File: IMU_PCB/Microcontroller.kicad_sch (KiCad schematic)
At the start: 17 parts, among them J4 Conn_01x02_Pin, M3 MountingHole, M3_1 MountingHole, U2 ESP32-DEVKIT-C, U3 TJA1050T/CM,118

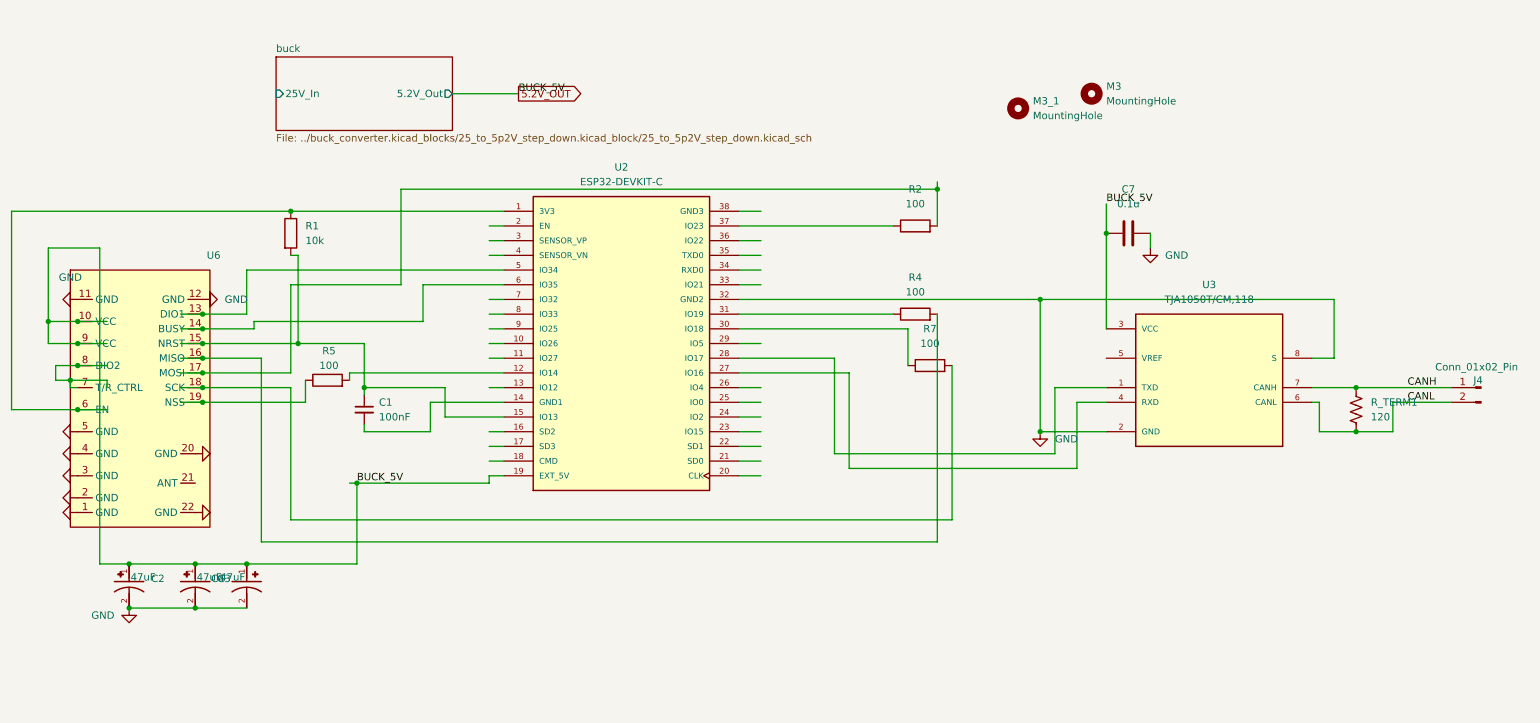
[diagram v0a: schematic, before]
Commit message: updated Julias IMU to use the revised buck converter and connectors. made the back plane mostly a ground plane (for the buck converter)
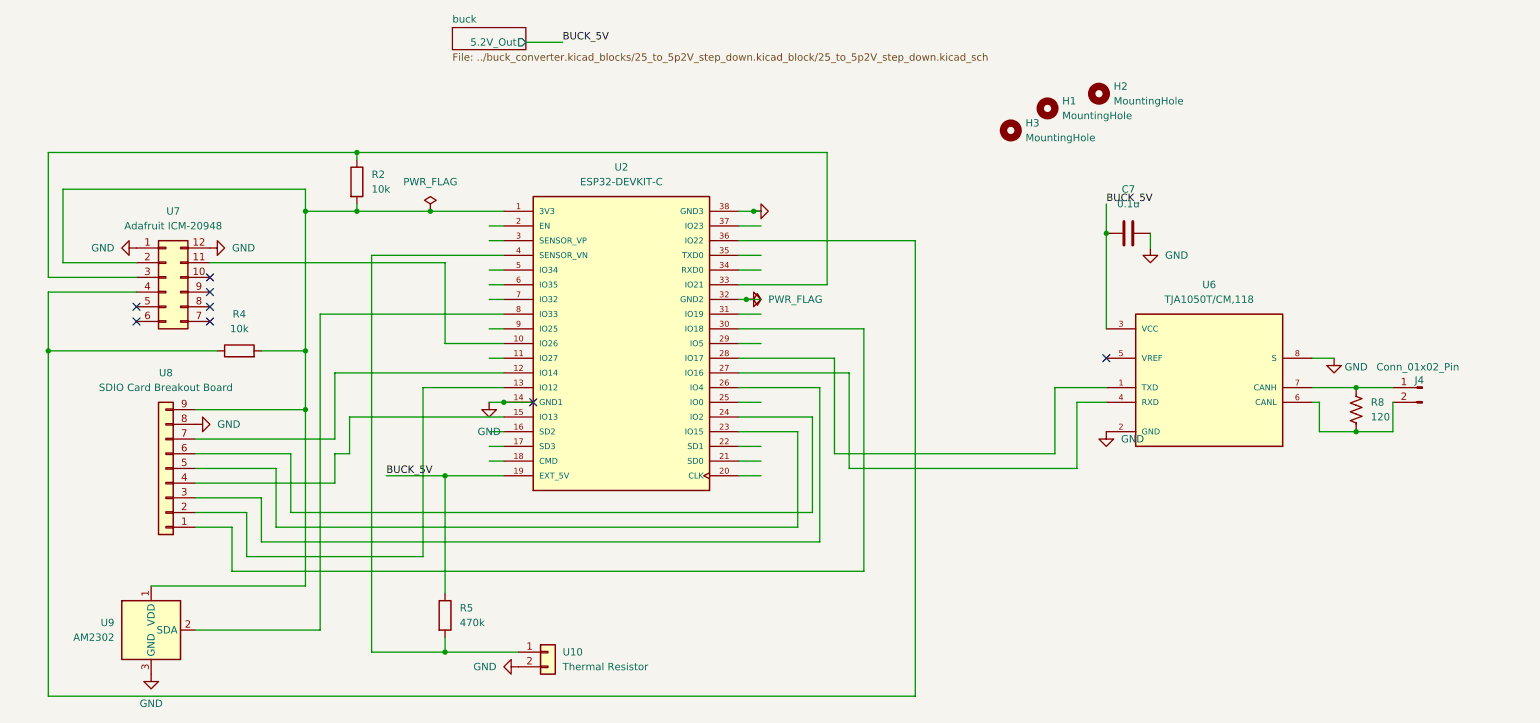
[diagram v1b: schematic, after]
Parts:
- removed C1: 100nF, Capacitor_SMD:C_1206_3216Metric_Pad1.33x1.80mm_HandSolder, symbol Device:C_Small
- removed C2, C3, C4: 47uF, Capacitor_Tantalum_SMD:CP_EIA-3528-21_Kemet-B_HandSolder, symbol 10TPE47MAZB:10TPE47MAZB
- removed M3, M3_1: MountingHole, MountingHole:MountingHole_3.2mm_M3, symbol Mechanical:MountingHole
- removed R1: 10k, Resistor_SMD:R_1206_3216Metric_Pad1.30x1.75mm_HandSolder, symbol Device:R
- removed R7: 100, Resistor_SMD:R_1206_3216Metric_Pad1.30x1.75mm_HandSolder, symbol Device:R
- removed U6: (no value), PROVE-footprints:E22P-915M30S, symbol telem_linsym:E22P-915M30S
- added H1, H2, H3: MountingHole, MountingHole:MountingHole_3.2mm_M3, symbol Mechanical:MountingHole
- added U10: Thermal Resistor, TerminalBlock_RND:TerminalBlock_RND_205-00232_1x02_P5.08mm_Horizontal, symbol Connector_Generic:Conn_01x02
- added U7: Adafruit ICM-20948, PROVE-footprints:Adafruit_ICM20948_2x6_Module, symbol Connector_Generic:Conn_02x06_Counter_Clockwise
- added U8: SDIO Card Breakout Board, Connector_PinHeader_2.54mm:PinHeader_1x09_P2.54mm_Vertical, symbol Connector_Generic:Conn_01x09
- added U9: AM2302, Sensor:ASAIR_AM2302_P2.54mm_Vertical, symbol Sensor:AM2302
- R2, R4: value 100 -> 10k; footprint Resistor_SMD:R_1206_3216Metric_Pad1.30x1.75mm_HandSolder -> Resistor_SMD:R_0805_2012Metric
- R5: value 100 -> 470k; footprint Resistor_SMD:R_1206_3216Metric_Pad1.30x1.75mm_HandSolder -> Resistor_SMD:R_0805_2012Metric
- U2: MANUFACTURER (none) -> ESPRESSIF
- U6: renamed from U3; MANUFACTURER (none) -> NXP USA
- renumbered R_TERM1 to R8
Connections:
- net 5.2V_OUT is gone; now on net BUCK_5V: C7.2, U2.19 (EXT_5V), U6.3 (VCC)
- net GND: now also U2.14 (GND1), U2.38 (GND3), U10.2 (Pin_2), U7.1 (Pin_1), U7.12 (Pin_12), U8.8 (Pin_8), U9.3 (GND), U9.4 (GND)
- net at U2.1 (3V3): now also R2.2, R4.2, U7.2 (Pin_2), U8.9 (Pin_9), U9.1 (VDD)
- net at U2.15 (IO13): now also U8.4 (Pin_4)
- net BUCK_5V: now reaches R5.1
- net at R2.1: now also U2.33 (IO21), U7.3 (Pin_3); no longer U2.37 (IO23)
- net at U2.30 (IO18): now also U8.1 (Pin_1)
- net at U2.12 (IO14): now also U8.7 (Pin_7); no longer R5.2
- net at U2.10 (IO26): now also U7.11 (Pin_11)
- net at U2.13 (IO12): now also U8.2 (Pin_2)
- net at U2.23 (IO15): now also U8.5 (Pin_5)
- net at U2.24 (IO2): now also U8.6 (Pin_6)
- net at U2.26 (IO4): now also U8.3 (Pin_3)
- net at R4.1: now also U2.36 (IO22), U7.4 (Pin_4); no longer U2.31 (IO19)
- net at U2.4 (SENSOR_VN): now also R5.2, U10.1 (Pin_1)
- net at U2.8 (IO33): now also U9.2 (SDA)
- net CANH: no longer names the net of J4.1 (Pin_1), R8.1, U6.7 (CANH)
- net CANL: no longer names the net of J4.2 (Pin_2), R8.2, U6.6 (CANL)
- no-connect marks 0 -> 8
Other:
- sheet buck ports: added none; removed 25V_In
- company: (none) -> PROVE Lab, Julia Kohrt
- title: (none) -> IMU Board
- moved on the sheet: J4

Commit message: small updates to buck, fixed vias, and remove connection to input connector ground pad
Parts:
- removed H2: MountingHole, MountingHole:MountingHole_3.2mm_M3, symbol Mechanical:MountingHole
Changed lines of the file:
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@@
-	(symbol
-		(lib_id "Mechanical:MountingHole")
-		(at 203.2 88.9 0)
-		(unit 1)
-		(body_style 1)
-		(exclude_from_sim no)
-		(in_bom no)
-		(on_board yes)
-		(in_pos_files yes)
-		(dnp no)
-		(fields_autoplaced yes)
-		(property "Reference" "H2"
-			(at 205.74 87.6299 0)
-			(show_name no)
-			(do_not_autoplace no)
-			(effects
-				(font
-					(size 1.27 1.27)
-				)
-				(justify left)
-			)
-		)
-		(property "Value" "MountingHole"
-			(at 205.74 90.1699 0)
-			(show_name no)
-			(do_not_autoplace no)
-			(effects
-				(font
-					(size 1.27 1.27)
-				)
-				(justify left)
-			)
-		)
-		(property "Footprint" "MountingHole:MountingHole_3.2mm_M3"
-			(at 203.2 88.9 0)
-			(hide yes)
-			(show_name no)
-			(do_not_autoplace no)
-			(effects
-				(font
-					(size 1.27 1.27)
-				)
-			)
-		)
-		(property "Datasheet" ""
-			(at 203.2 88.9 0)
-			(hide yes)
-			(show_name no)
-			(do_not_autoplace no)
-			(effects
-				(font
-					(size 1.27 1.27)
-				)
-			)
-		)
-		(property "Description" "Mounting Hole without connection"
-			(at 203.2 88.9 0)
-			(hide yes)
-			(show_name no)
-			(do_not_autoplace no)
-			(effects
-				(font
-					(size 1.27 1.27)
-				)
-			)
-		)
-		(instances
-			(project "Microcontroller"
-				(path "/c58806c5-432f-4c41-8983-8e5fd30a3703"
-					(reference "H2")
-					(unit 1)
-				)
-			)
-		)
-	)
 	(symbol
 		(lib_id "Mechanical:MountingHole")
